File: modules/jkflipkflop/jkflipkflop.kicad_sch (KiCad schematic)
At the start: 1 part, among them J1 Conn_02x18_Counter_Clockwise

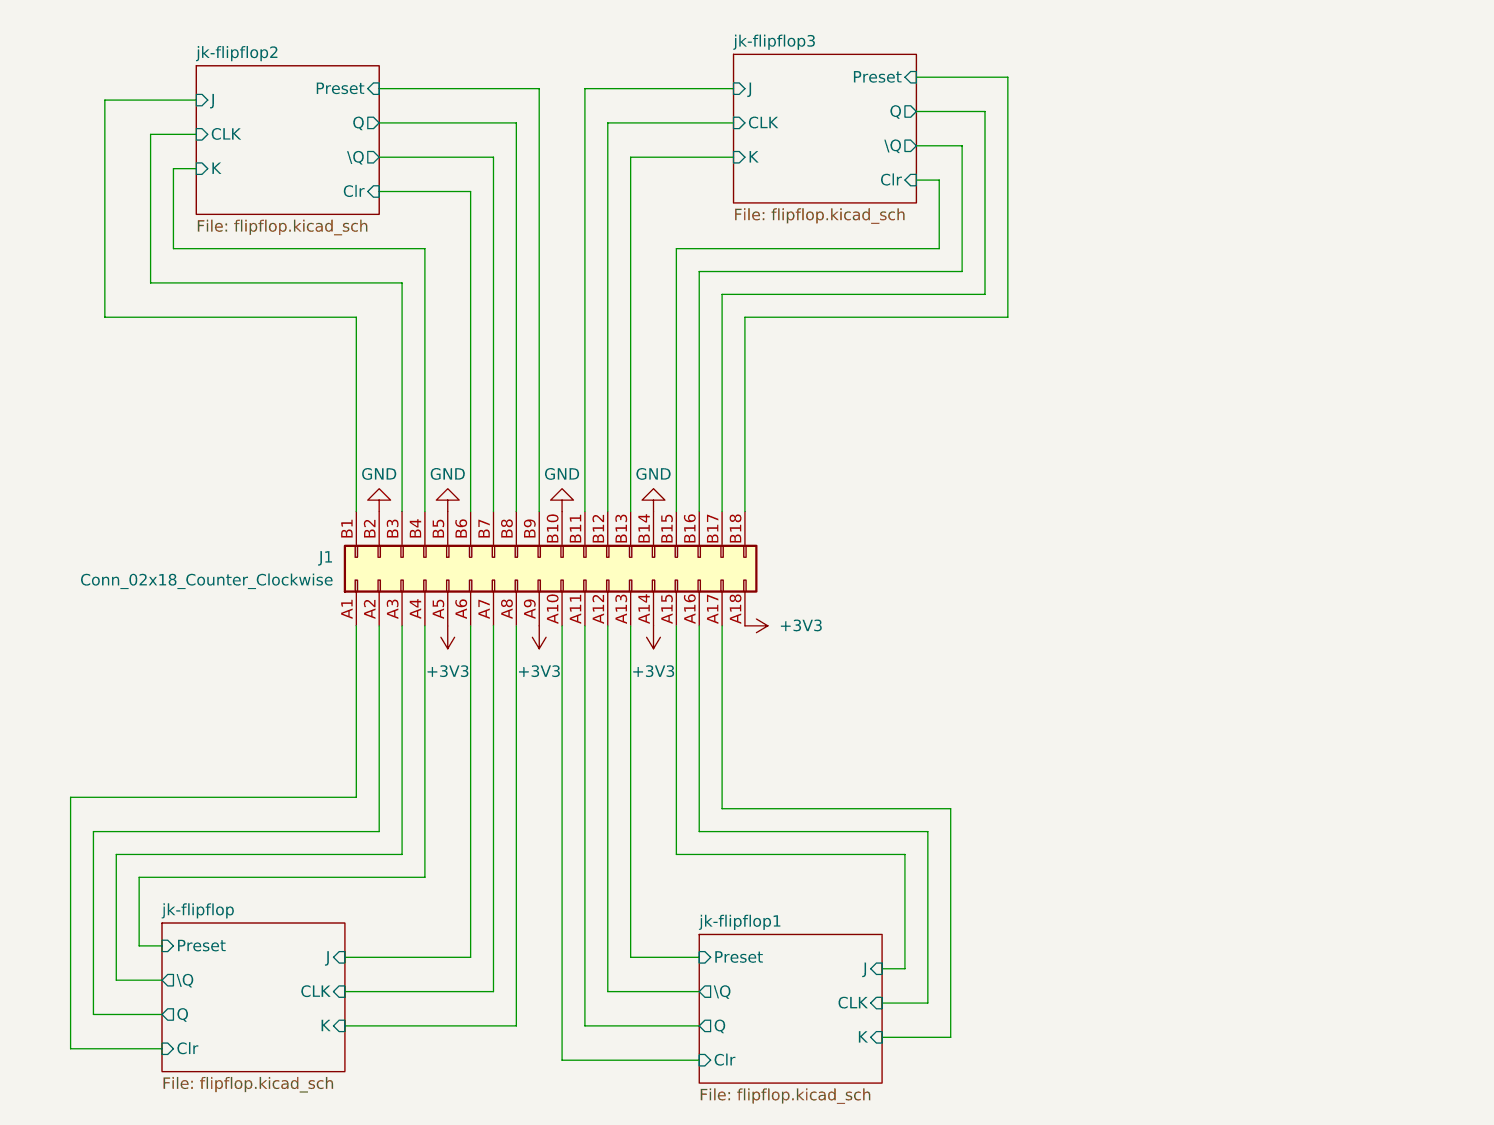
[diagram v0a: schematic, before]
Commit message: changed from pcie x1 to mini pcie. added 2 flipflops
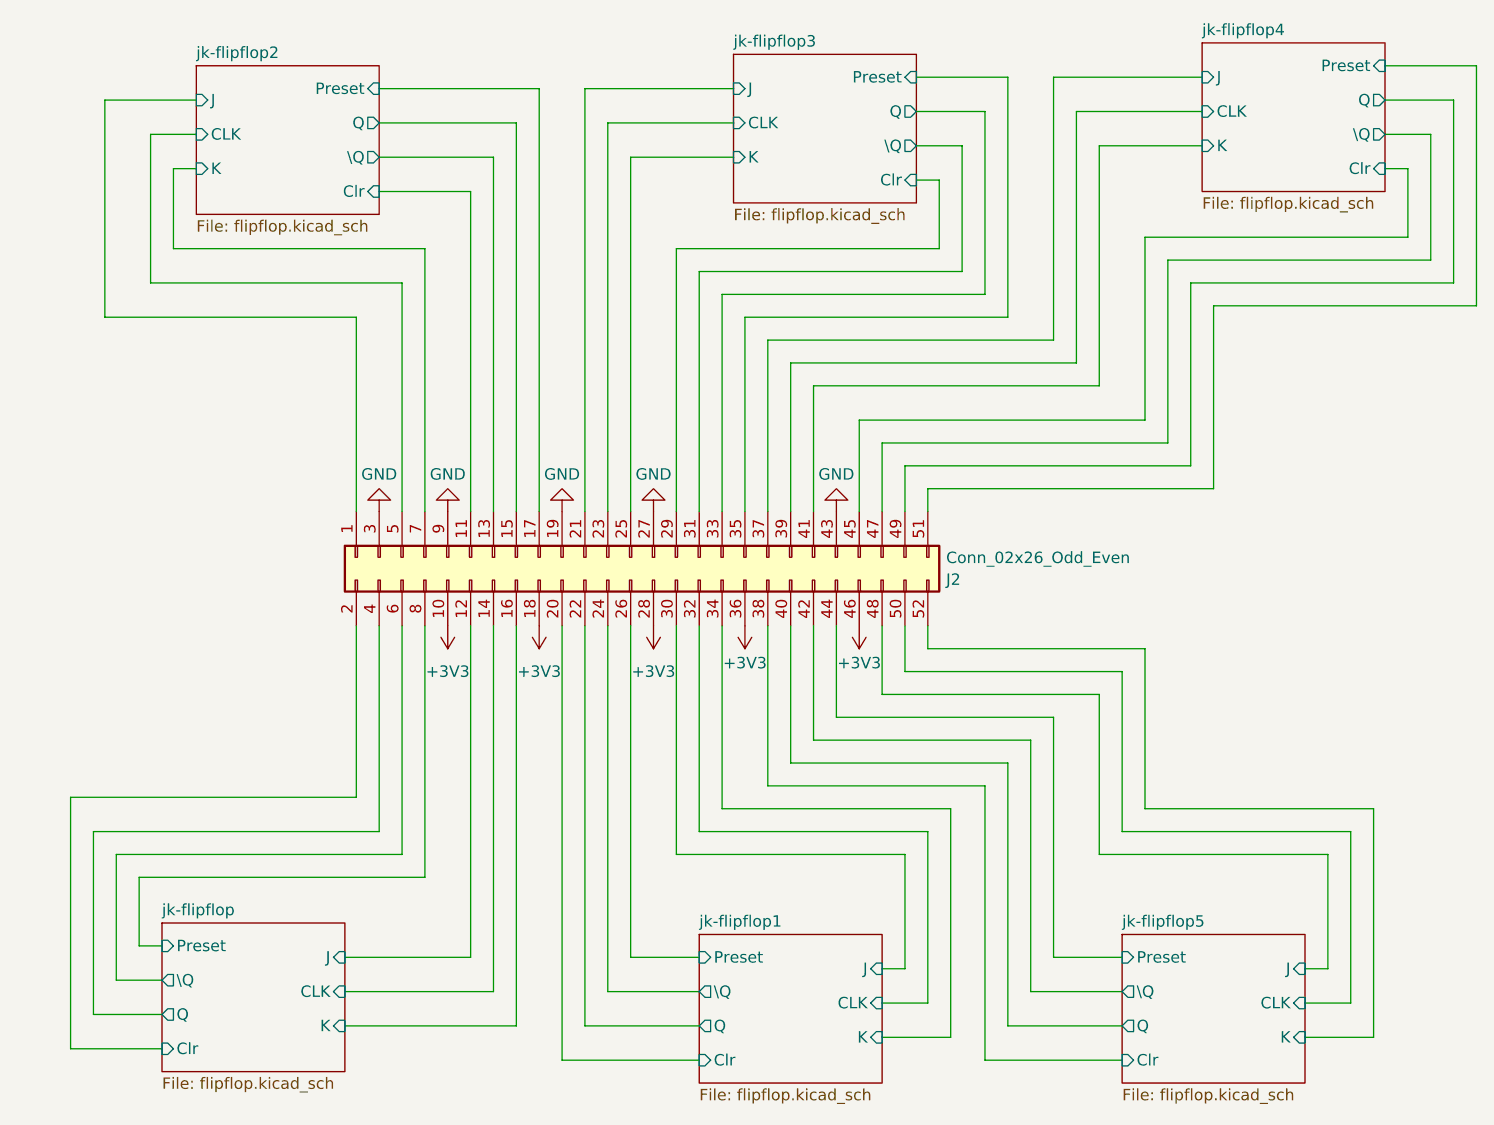
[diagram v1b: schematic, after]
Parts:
- removed J1: Conn_02x18_Counter_Clockwise, Connector_PCBEdge:BUS_PCIexpress_x1, symbol Connector_Generic:Conn_02x18_Counter_Clockwise
- added J2: Conn_02x26_Odd_Even, mpcie:mpcie-full-card, symbol Connector_Generic:Conn_02x26_Odd_Even
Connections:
- net +3V3: now also J2.10 (Pin_10), J2.18 (Pin_18), J2.28 (Pin_28), J2.36 (Pin_36), J2.46 (Pin_46)
- net GND: now also J2.19 (Pin_19), J2.27 (Pin_27), J2.3 (Pin_3), J2.43 (Pin_43), J2.9 (Pin_9)
- net jk-flipflop/CLK: now also J2.14 (Pin_14)
- net jk-flipflop/Clr: now also J2.2 (Pin_2)
- net jk-flipflop/J: now also J2.12 (Pin_12)
- net jk-flipflop/K: now also J2.16 (Pin_16)
- net jk-flipflop/Preset: now also J2.8 (Pin_8)
- net jk-flipflop/Q: now also J2.4 (Pin_4)
- net jk-flipflop/\Q: now also J2.6 (Pin_6)
- net jk-flipflop1/CLK: now also J2.32 (Pin_32)
- net jk-flipflop1/Clr: now also J2.20 (Pin_20)
- net jk-flipflop1/J: now also J2.30 (Pin_30)
- net jk-flipflop1/K: now also J2.34 (Pin_34)
- net jk-flipflop1/Preset: now also J2.26 (Pin_26)
- net jk-flipflop1/Q: now also J2.22 (Pin_22)
- net jk-flipflop1/\Q: now also J2.24 (Pin_24)
- net jk-flipflop2/CLK: now also J2.5 (Pin_5)
- net jk-flipflop2/Clr: now also J2.11 (Pin_11)
- net jk-flipflop2/J: now also J2.1 (Pin_1)
- net jk-flipflop2/K: now also J2.7 (Pin_7)
- net jk-flipflop2/Preset: now also J2.17 (Pin_17)
- net jk-flipflop2/Q: now also J2.15 (Pin_15)
- net jk-flipflop2/\Q: now also J2.13 (Pin_13)
- net jk-flipflop3/CLK: now also J2.23 (Pin_23)
- net jk-flipflop3/Clr: now also J2.29 (Pin_29)
- net jk-flipflop3/J: now also J2.21 (Pin_21)
- net jk-flipflop3/K: now also J2.25 (Pin_25)
- net jk-flipflop3/Preset: now also J2.35 (Pin_35)
- net jk-flipflop3/Q: now also J2.33 (Pin_33)
- net jk-flipflop3/\Q: now also J2.31 (Pin_31)
- new net jk-flipflop4/CLK: J2.39 (Pin_39)
- new net jk-flipflop4/Clr: J2.45 (Pin_45)
- new net jk-flipflop4/J: J2.37 (Pin_37)
- new net jk-flipflop4/K: J2.41 (Pin_41)
- new net jk-flipflop4/Preset: J2.51 (Pin_51)
- new net jk-flipflop4/Q: J2.49 (Pin_49)
- new net jk-flipflop4/\Q: J2.47 (Pin_47)
- new net jk-flipflop5/CLK: J2.50 (Pin_50)
- new net jk-flipflop5/Clr: J2.38 (Pin_38)
- new net jk-flipflop5/J: J2.48 (Pin_48)
- new net jk-flipflop5/K: J2.52 (Pin_52)
- new net jk-flipflop5/Preset: J2.44 (Pin_44)
- new net jk-flipflop5/Q: J2.40 (Pin_40)
- new net jk-flipflop5/\Q: J2.42 (Pin_42)
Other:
- added sheet jk-flipflop4 (flipflop.kicad_sch)
- added sheet jk-flipflop5 (flipflop.kicad_sch)

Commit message: flipflop fab output
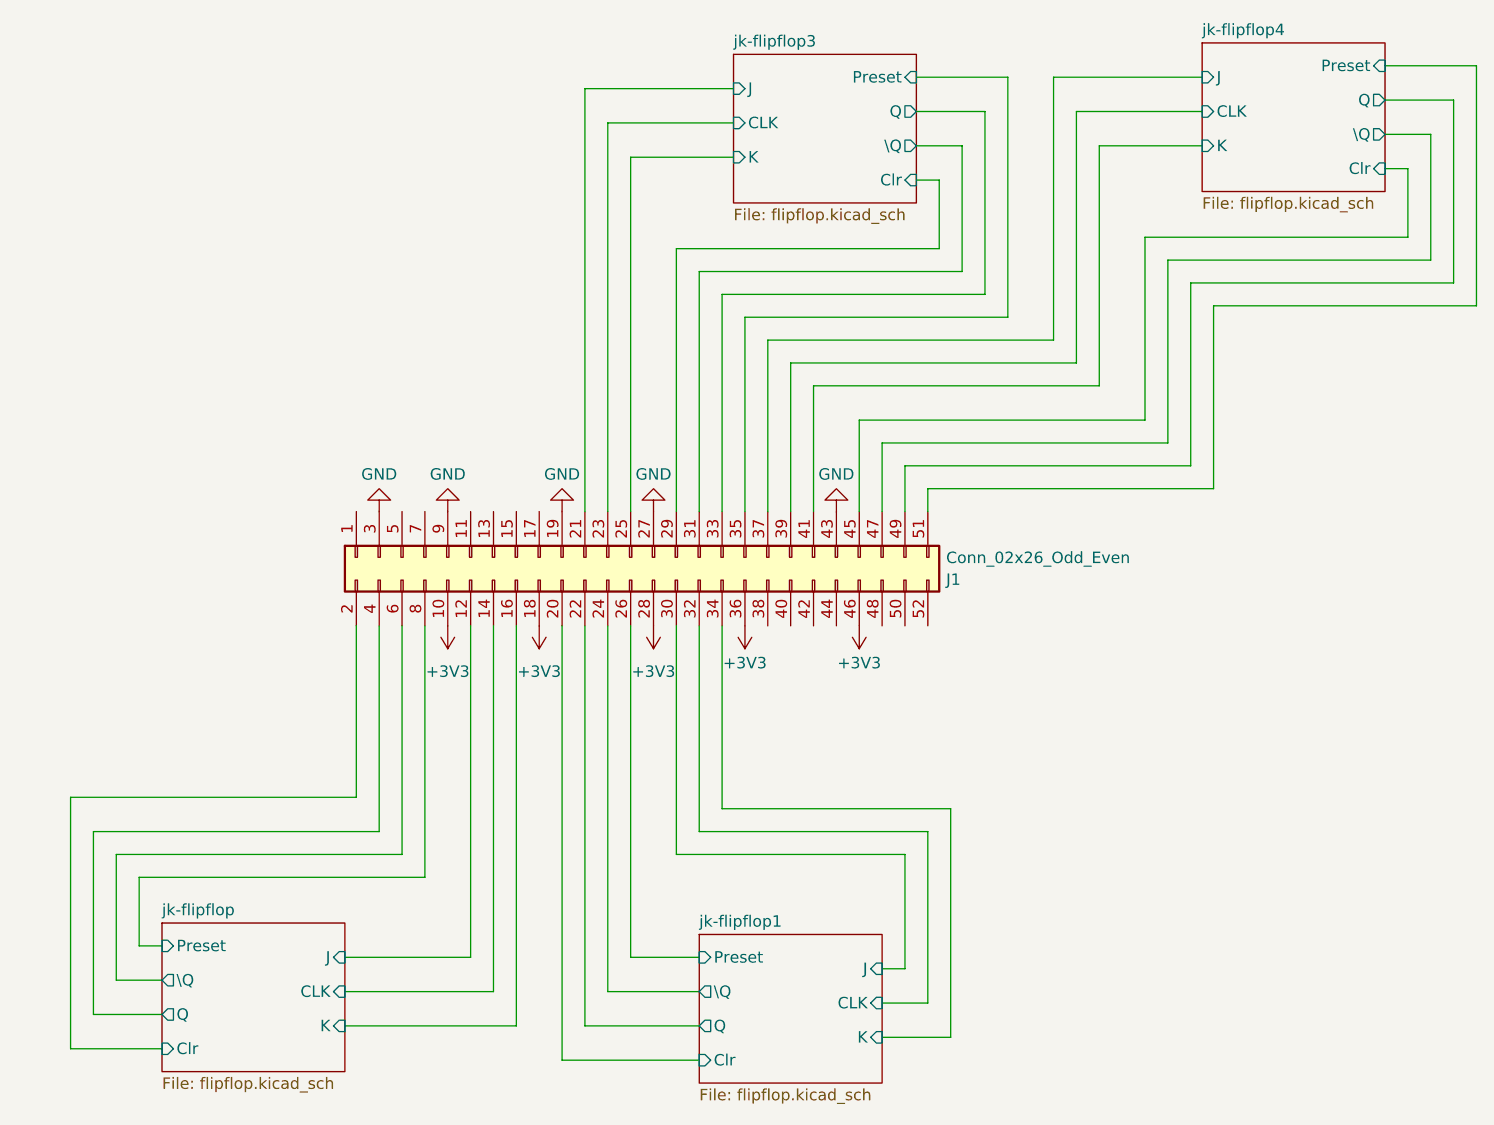
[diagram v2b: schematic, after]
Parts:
- J1: renamed from J2; now left out of the parts list
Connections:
- net jk-flipflop2/CLK: no longer names the net of J1.5 (Pin_5)
- net jk-flipflop2/Clr: no longer names the net of J1.11 (Pin_11)
- net jk-flipflop2/J: no longer names the net of J1.1 (Pin_1)
- net jk-flipflop2/K: no longer names the net of J1.7 (Pin_7)
- net jk-flipflop2/Preset: no longer names the net of J1.17 (Pin_17)
- net jk-flipflop2/Q: no longer names the net of J1.15 (Pin_15)
- net jk-flipflop2/\Q: no longer names the net of J1.13 (Pin_13)
- net jk-flipflop5/CLK: no longer names the net of J1.50 (Pin_50)
- net jk-flipflop5/Clr: no longer names the net of J1.38 (Pin_38)
- net jk-flipflop5/J: no longer names the net of J1.48 (Pin_48)
- net jk-flipflop5/K: no longer names the net of J1.52 (Pin_52)
- net jk-flipflop5/Preset: no longer names the net of J1.44 (Pin_44)
- net jk-flipflop5/Q: no longer names the net of J1.40 (Pin_40)
- net jk-flipflop5/\Q: no longer names the net of J1.42 (Pin_42)
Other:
- removed sheet jk-flipflop2
- removed sheet jk-flipflop5
